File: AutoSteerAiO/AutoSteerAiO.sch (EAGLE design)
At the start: 87 parts, among them K4 CB1A-P-12V, U1 VX7805-1000

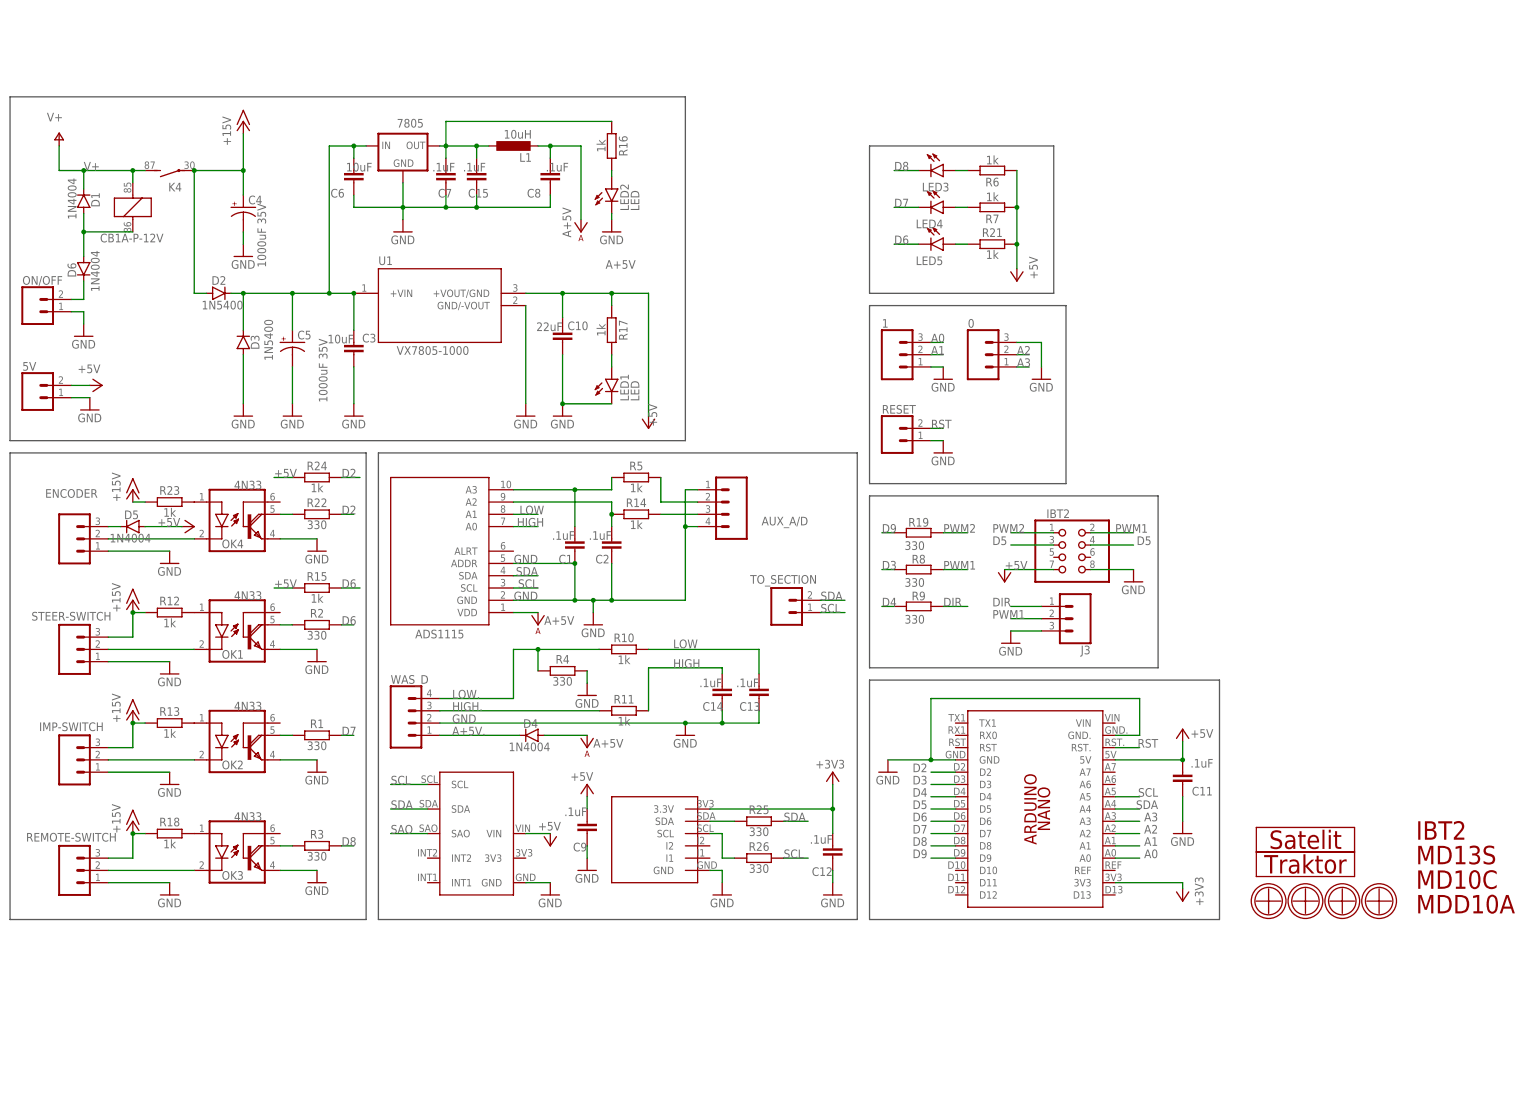
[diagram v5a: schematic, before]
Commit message: Add files via upload
I removed the reset connector from PCB since the arduino nano has an ICSP header on which there is a reset pin, and added the capacitor 1000uF for WAS
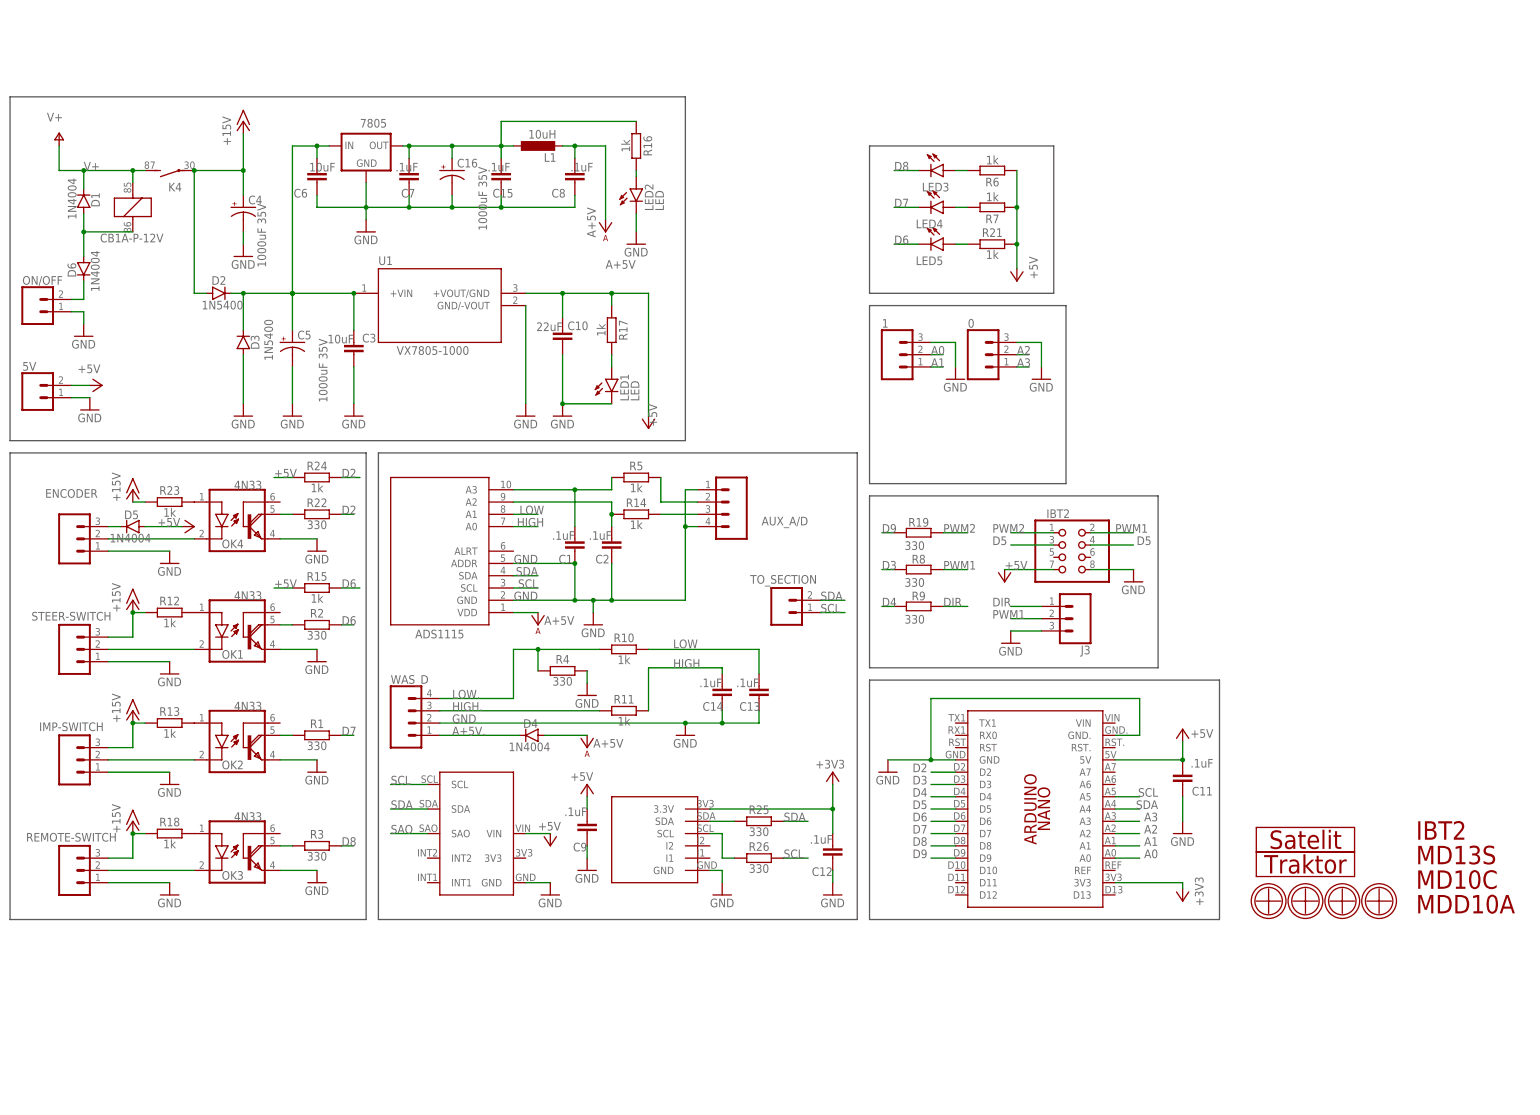
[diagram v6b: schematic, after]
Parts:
- removed RESET: CONNECTOR 1x2 PINS, SparkFun-Connectors:CONN_02
- added C16: 1000uF 35V, SparkFun-Capacitors:1000UF-RADIAL-5MM-25V-20%
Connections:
- removed net RST: PCB1.RST., RESET.2
- net A0: now also 1.2; no longer 1.3
- net A1: now also 1.1; no longer 1.2
- net GND: now also 1.3, C16.-; no longer 1.1, RESET.1
- net N$25: now also C16.+
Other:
- moved on the sheet: 7805, C15, C6, C7, C8, L1, LED2, R16

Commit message: Add files via upload
Add connector for 15v
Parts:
- added 15V: CONNECTOR 1x2 PINS, SparkFun-Connectors:CONN_02
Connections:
- net +15V: now also 15V.2
- net GND: now also 15V.1
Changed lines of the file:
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@@
 <?xml version="1.0" encoding="utf-8"?>
 <!DOCTYPE eagle SYSTEM "eagle.dtd">
-<eagle version="9.4.0">
+<eagle version="9.3.2">
 <drawing>
 <settings>
@@
 <setting verticaltext="up"/>
 </settings>
-<grid distance="0.1" unitdist="inch" unit="inch" style="lines" multiple="1" display="no" altdistance="0.01" altunitdist="inch" altunit="inch"/>
+<grid distance="0.1" unitdist="inch" unit="mil" style="lines" multiple="1" display="no" altdistance="50" altunitdist="mil" altunit="mil"/>
 <layers>
 <layer number="1" name="Top" color="4" fill="1" visible="no" active="no"/>
@@
 <attribute name="OC_NEWARK" value="unknown"/>
 </part>
+<part name="15V" library="SparkFun-Connectors" library_urn="urn:adsk.eagle:library:513" deviceset="CONN_02" device="" package3d_urn="urn:adsk.eagle:package:38039/1" value="CONNECTOR 1x2 PINS">
+<attribute name="MF" value=""/>
+<attribute name="MPN" value=""/>
+<attribute name="OC_NEWARK" value="unknown"/>
+</part>
+<part name="P+4" library="supply1" library_urn="urn:adsk.eagle:library:371" deviceset="+15V" device=""/>
+<part name="GND9" library="supply1" library_urn="urn:adsk.eagle:library:371" deviceset="GND" device=""/>
 </parts>
 <sheets>
@@
 <attribute name="MPN" x="73.66" y="256.54" size="1.778" layer="96" display="off"/>
 </instance>
+<instance part="15V" gate="G$1" x="7.62" y="209.55" smashed="yes">
+<attribute name="NAME" x="5.08" y="215.138" size="1.778" layer="95" font="vector"/>
+<attribute name="OC_NEWARK" x="7.62" y="209.55" size="1.778" layer="96" display="off"/>
+<attribute name="MF" x="7.62" y="209.55" size="1.778" layer="96" display="off"/>
+<attribute name="MPN" x="7.62" y="209.55" size="1.778" layer="96" display="off"/>
+</instance>
+<instance part="P+4" gate="1" x="21.59" y="212.09" smashed="yes" rot="R270">
+<attribute name="VALUE" x="16.51" y="214.63" size="1.778" layer="96"/>
+</instance>
+<instance part="GND9" gate="1" x="19.05" y="207.01" smashed="yes">
+<attribute name="VALUE" x="16.51" y="204.47" size="1.778" layer="96"/>
+</instance>
 </instances>
 <busses>
@@
 <wire x1="15.24" y1="177.8" x2="2.54" y2="177.8" width="0.1524" layer="91"/>
 </segment>
+<segment>
+<pinref part="15V" gate="G$1" pin="1"/>
+<wire x1="15.24" y1="209.55" x2="19.05" y2="209.55" width="0.1524" layer="91"/>
+<pinref part="GND9" gate="1" pin="GND"/>
+</segment>
 </net>
 <net name="D5" class="0">
@@
 <pinref part="P+12" gate="1" pin="+15V"/>
 </segment>
+<segment>
+<pinref part="15V" gate="G$1" pin="2"/>
+<wire x1="15.24" y1="212.09" x2="19.05" y2="212.09" width="0.1524" layer="91"/>
+<pinref part="P+4" gate="1" pin="+15V"/>
+</segment>
 </net>
